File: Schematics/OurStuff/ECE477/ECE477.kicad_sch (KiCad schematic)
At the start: 67 parts, among them J1 USB_B_Micro, J2 Barrel_Jack, J3 OLED JST PH 7pin, J4 Microphone Connector, J5 UART_Conn, J6 Debug Conn, J7 D30V30F3, Q1 SS8050-G, Q2 SS8050-G, SW1 Boot Button, SW2 RST Button, SW3 Button 1, SW4 Button 2, U1 ESP32-WROOM-32E, U2 CP2102N-Axx-xQFN28

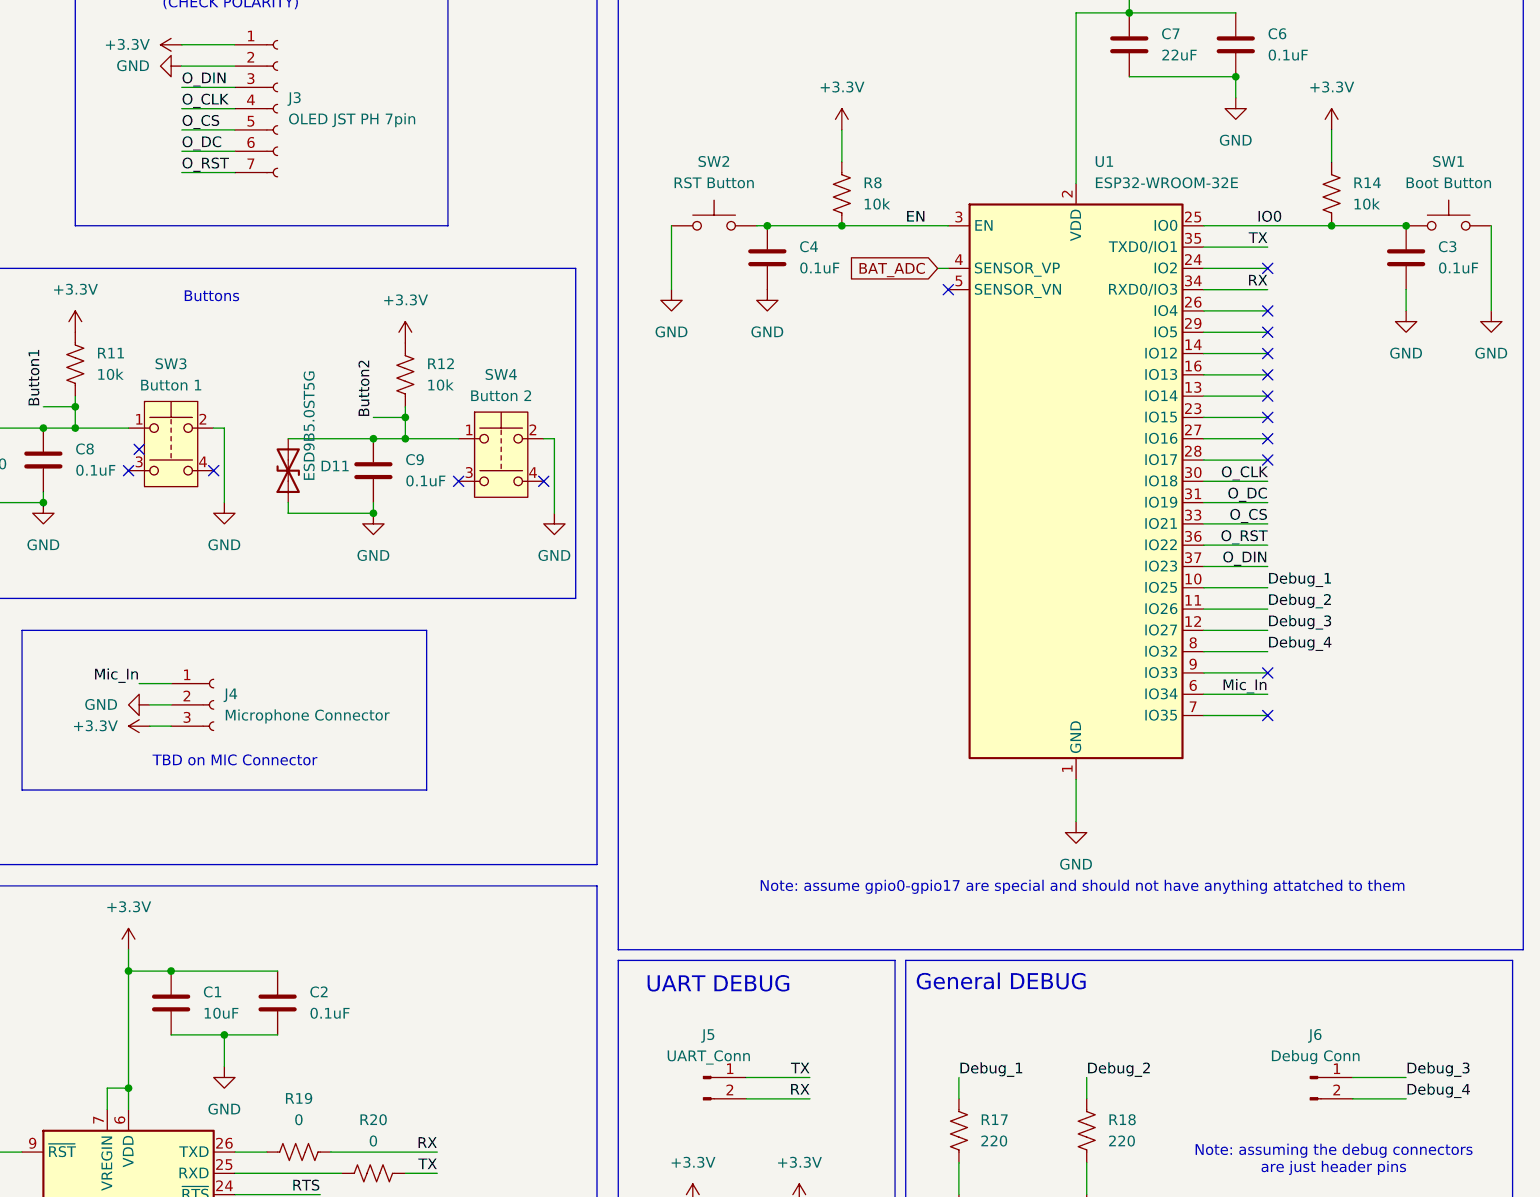
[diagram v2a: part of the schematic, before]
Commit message: Started layout
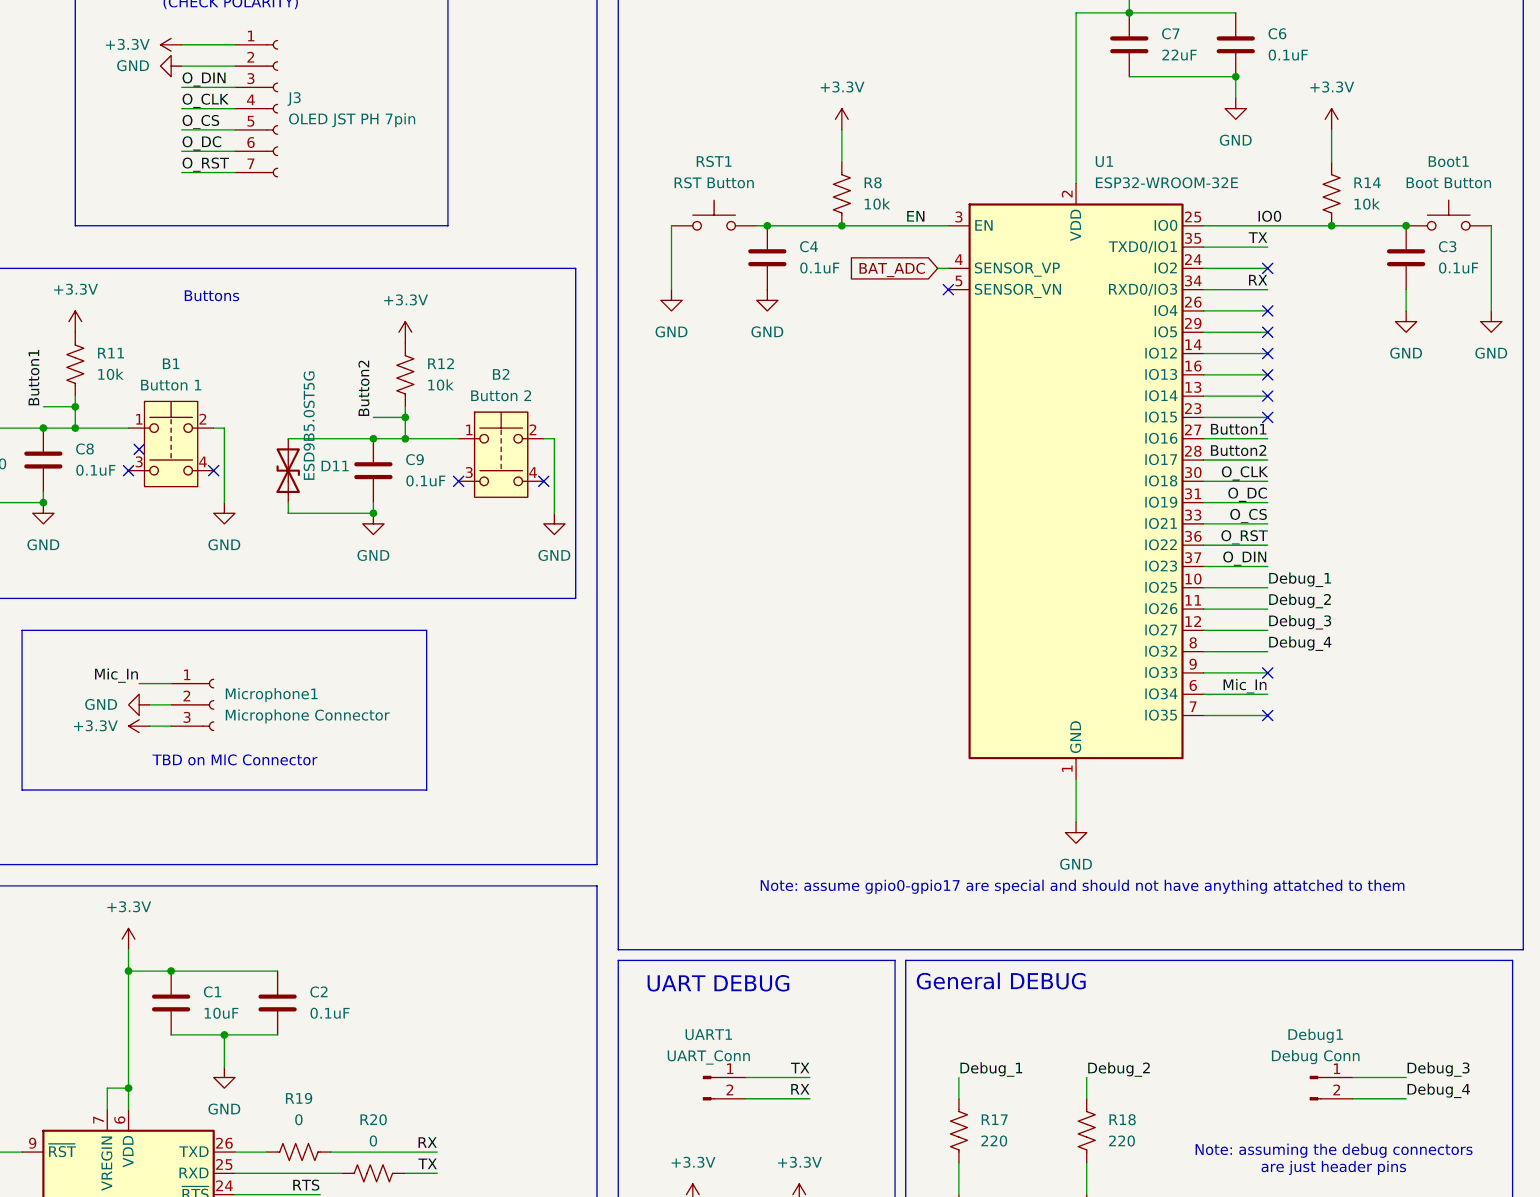
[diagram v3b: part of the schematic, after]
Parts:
- renumbered SW3 to B1, SW4 to B2, SW1 to Boot1, J6 to Debug1, J4 to Microphone1, SW2 to RST1, J5 to UART1
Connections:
- net Button1: now also U1.27 (IO16)
- net Button2: now also U1.28 (IO17)
- no-connect marks 32 -> 30
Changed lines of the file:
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@@
 	)
 	(no_connect
-		(at 375.92 80.01)
-	)
-	(no_connect
 		(at 252.73 208.28)
 	)
@@
 	)
 	(no_connect
-		(at 375.92 82.55)
-	)
-	(no_connect
 		(at 375.92 59.69)
 	)
@@
 		)
 	)
+	(label "Button2"
+		(at 375.92 82.55 180)
+		(fields_autoplaced yes)
+		(effects
+			(font
+				(size 1.27 1.27)
+			)
+			(justify right bottom)
+		)
+	)
 	(label "USB_DN"
 		(at 180.34 219.71 0)
@@
 		)
 	)
+	(label "Button1"
+		(at 375.92 80.01 180)
+		(fields_autoplaced yes)
+		(effects
+			(font
+				(size 1.27 1.27)
+			)
+			(justify right bottom)
+		)
+	)
 	(label "Debug_4"
 		(at 375.92 105.41 0)
@@
 		(dnp no)
 		(fields_autoplaced yes)
-		(property "Reference" "SW1"
+		(property "Reference" "Boot1"
 			(at 397.51 46.99 0)
 			(effects
@@
 			(project ""
 				(path "/f5b3def7-e561-4cb3-8a45-4eba76d025b6"
-					(reference "SW1")
+					(reference "Boot1")
 					(unit 1)
 				)
@@
 		(dnp no)
 		(fields_autoplaced yes)
-		(property "Reference" "SW3"
+		(property "Reference" "B1"
 			(at 245.11 71.12 0)
 			(effects
@@
 			(project ""
 				(path "/f5b3def7-e561-4cb3-8a45-4eba76d025b6"
-					(reference "SW3")
+					(reference "B1")
 					(unit 1)
 				)
@@
 		(dnp no)
 		(fields_autoplaced yes)
-		(property "Reference" "J4"
+		(property "Reference" "Microphone1"
 			(at 251.46 110.4899 0)
 			(effects
@@
 			(project ""
 				(path "/f5b3def7-e561-4cb3-8a45-4eba76d025b6"
-					(reference "J4")
+					(reference "Microphone1")
 					(unit 1)
 				)
@@
 		(dnp no)
 		(fields_autoplaced yes)
-		(property "Reference" "SW4"
+		(property "Reference" "B2"
 			(at 284.48 72.39 0)
 			(effects
@@
 			(project "ECE477"
 				(path "/f5b3def7-e561-4cb3-8a45-4eba76d025b6"
-					(reference "SW4")
+					(reference "B2")
 					(unit 1)
 				)
@@
 		(dnp no)
 		(fields_autoplaced yes)
-		(property "Reference" "J5"
+		(property "Reference" "UART1"
 			(at 309.245 151.13 0)
 			(effects
@@
 			(project ""
 				(path "/f5b3def7-e561-4cb3-8a45-4eba76d025b6"
-					(reference "J5")
+					(reference "UART1")
 					(unit 1)
 				)
@@
 		(dnp no)
 		(fields_autoplaced yes)
-		(property "Reference" "J6"
+		(property "Reference" "Debug1"
 			(at 381.635 151.13 0)
 			(effects
@@
 			(project "ECE477"
 				(path "/f5b3def7-e561-4cb3-8a45-4eba76d025b6"
-					(reference "J6")
+					(reference "Debug1")
 					(unit 1)
 				)
@@
 		(dnp no)
 		(fields_autoplaced yes)
-		(property "Reference" "SW2"
+		(property "Reference" "RST1"
 			(at 309.88 46.99 0)
 			(effects
@@
 			(project "ECE477"
 				(path "/f5b3def7-e561-4cb3-8a45-4eba76d025b6"
-					(reference "SW2")
+					(reference "RST1")
 					(unit 1)
 				)

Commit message: started routing 💢
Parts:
- removed TP10: IO0, TestPoint:TestPoint_Keystone_5010-5014_Multipurpose, symbol Connector:TestPoint
- removed TP9: EN, TestPoint:TestPoint_Keystone_5010-5014_Multipurpose, symbol Connector:TestPoint
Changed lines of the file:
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@@
 	(wire
 		(pts
-			(xy 386.08 243.84) (xy 394.97 243.84)
-		)
-		(stroke
-			(width 0)
-			(type default)
-		)
-	)
-	(wire
-		(pts
 			(xy 368.3 95.25) (xy 375.92 95.25)
 		)
@@
 	(wire
 		(pts
-			(xy 386.08 236.22) (xy 394.97 236.22)
-		)
-		(stroke
-			(width 0)
-			(type default)
-		)
-	)
-	(wire
-		(pts
 			(xy 368.3 100.33) (xy 375.92 100.33)
 		)
@@
 		)
 	)
-	(label "EN"
-		(at 394.97 236.22 180)
-		(fields_autoplaced yes)
-		(effects
-			(font
-				(size 1.27 1.27)
-			)
-			(justify right bottom)
-		)
-	)
 	(label "O_CLK"
 		(at 375.92 85.09 180)
@@
 		)
 	)
-	(label "IO0"
-		(at 394.97 243.84 180)
-		(fields_autoplaced yes)
-		(effects
-			(font
-				(size 1.27 1.27)
-			)
-			(justify right bottom)
-		)
-	)
 	(label "Button1"
 		(at 229.87 76.2 90)
@@
 	)
 	(symbol
-		(lib_id "Connector:TestPoint")
-		(at 386.08 243.84 90)
-		(unit 1)
-		(exclude_from_sim no)
-		(in_bom yes)
-		(on_board yes)
-		(dnp no)
-		(fields_autoplaced yes)
-		(property "Reference" "TP10"
-			(at 382.778 238.76 90)
-			(effects
-				(font
-					(size 1.27 1.27)
-				)
-			)
-		)
-		(property "Value" "IO0"
-			(at 382.778 241.3 90)
-			(effects
-				(font
-					(size 1.27 1.27)
-				)
-			)
-		)
-		(property "Footprint" "TestPoint:TestPoint_Keystone_5010-5014_Multipurpose"
-			(at 386.08 238.76 0)
-			(effects
-				(font
-					(size 1.27 1.27)
-				)
-				(hide yes)
-			)
-		)
-		(property "Datasheet" "~"
-			(at 386.08 238.76 0)
-			(effects
-				(font
-					(size 1.27 1.27)
-				)
-				(hide yes)
-			)
-		)
-		(property "Description" "test point"
-			(at 386.08 243.84 0)
-			(effects
-				(font
-					(size 1.27 1.27)
-				)
-				(hide yes)
-			)
-		)
-		(pin "1"
-		)
-		(instances
-			(project "ECE477"
-				(path "/f5b3def7-e561-4cb3-8a45-4eba76d025b6"
-					(reference "TP10")
-					(unit 1)
-				)
-			)
-		)
-	)
-	(symbol
 		(lib_id "power:GND")
 		(at 265.43 190.5 90)
@@
 					(unit 1)
 				)
-			)
-		)
-	)
-	(symbol
-		(lib_id "Connector:TestPoint")
-		(at 386.08 236.22 90)
-		(unit 1)
-		(exclude_from_sim no)
-		(in_bom yes)
-		(on_board yes)
-		(dnp no)
-		(fields_autoplaced yes)
-		(property "Reference" "TP9"
-			(at 382.778 231.14 90)
-			(effects
-				(font
-					(size 1.27 1.27)
-				)
-			)
-		)
-		(property "Value" "EN"
-			(at 382.778 233.68 90)
-			(effects
-				(font
-					(size 1.27 1.27)
-				)
-			)
-		)
-		(property "Footprint" "TestPoint:TestPoint_Keystone_5010-5014_Multipurpose"
-			(at 386.08 231.14 0)
-			(effects
-				(font
-					(size 1.27 1.27)
-				)
-				(hide yes)
-			)
-		)
-		(property "Datasheet" "~"
-			(at 386.08 231.14 0)
-			(effects
-				(font
-					(size 1.27 1.27)
-				)
-				(hide yes)
-			)
-		)
-		(property "Description" "test point"
-			(at 386.08 236.22 0)
-			(effects
-				(font
-					(size 1.27 1.27)
-				)
-				(hide yes)
-			)
-		)
-		(pin "1"
-		)
-		(instances
-			(project "ECE477"
-				(path "/f5b3def7-e561-4cb3-8a45-4eba76d025b6"
-					(reference "TP9")
-					(unit 1)
-				)

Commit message: hell yeah
pcb complete ver 1 (no more deletes please)
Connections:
- net Gnd_Bat is gone; now on net GND: J2.2, J7.3 (Pin_3)
- net Button1: now also U1.10 (IO25); no longer U1.27 (IO16)
- net Button2: now also U1.11 (IO26); no longer U1.28 (IO17)
- net Debug_1: now also U1.28 (IO17); no longer U1.10 (IO25)
- net Debug_2: now also U1.27 (IO16); no longer U1.11 (IO26)
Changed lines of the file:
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@@
 	)
 	(junction
+		(at 186.69 41.91)
+		(diameter 0)
+		(color 0 0 0 0)
+	)
+	(junction
 		(at 269.24 88.9)
 		(diameter 0)
@@
 	(wire
 		(pts
+			(xy 186.69 41.91) (xy 189.23 41.91)
+		)
+		(stroke
+			(width 0)
+			(type default)
+		)
+	)
+	(wire
+		(pts
 			(xy 240.03 140.97) (xy 240.03 143.51)
 		)
@@
 	(wire
 		(pts
-			(xy 368.3 82.55) (xy 375.92 82.55)
+			(xy 368.3 82.55) (xy 377.19 82.55)
 		)
 		(stroke
@@
 	(wire
 		(pts
-			(xy 368.3 80.01) (xy 375.92 80.01)
+			(xy 368.3 80.01) (xy 377.19 80.01)
 		)
 		(stroke
@@
 	(wire
 		(pts
-			(xy 181.61 41.91) (xy 189.23 41.91)
+			(xy 181.61 41.91) (xy 186.69 41.91)
 		)
 		(stroke
@@
 	(label "RX"
 		(at 375.92 62.23 180)
-		(fields_autoplaced yes)
-		(effects
-			(font
-				(size 1.27 1.27)
-			)
-			(justify right bottom)
-		)
-	)
-	(label "Button2"
-		(at 375.92 82.55 180)
-		(fields_autoplaced yes)
 		(effects
 			(font
@@
 	(label "USB_DN"
 		(at 180.34 219.71 0)
-		(fields_autoplaced yes)
 		(effects
 			(font
@@
 	(label "TX"
 		(at 321.31 156.21 180)
-		(fields_autoplaced yes)
 		(effects
 			(font
@@
 	(label "TXT"
 		(at 307.34 195.58 180)
-		(fields_autoplaced yes)
 		(effects
 			(font
@@
 	(label "O_DC"
 		(at 375.92 87.63 180)
-		(fields_autoplaced yes)
 		(effects
 			(font
@@
 	(label "RXT"
 		(at 320.04 195.58 180)
-		(fields_autoplaced yes)
 		(effects
 			(font
@@
 	(label "Debug_2"
 		(at 354.33 156.21 0)
-		(fields_autoplaced yes)
 		(effects
 			(font
@@
 	(label "O_DIN"
 		(at 246.38 38.1 0)
-		(fields_autoplaced yes)
 		(effects
 			(font
@@
 	(label "RX"
 		(at 321.31 158.75 180)
-		(fields_autoplaced yes)
 		(effects
 			(font
@@
 		)
 	)
-	(label "Button1"
-		(at 375.92 80.01 180)
-		(fields_autoplaced yes)
+	(label "Debug_4"
+		(at 375.92 105.41 0)
 		(effects
 			(font
 				(size 1.27 1.27)
 			)
-			(justify right bottom)
+			(justify left bottom)
 		)
 	)
-	(label "Debug_4"
-		(at 375.92 105.41 0)
-		(fields_autoplaced yes)
+	(label "Debug_1"
+		(at 377.19 82.55 180)
 		(effects
 			(font
 				(size 1.27 1.27)
 			)
-			(justify left bottom)
+			(justify right bottom)
 		)
 	)
 	(label "Debug_4"
 		(at 392.43 158.75 0)
-		(fields_autoplaced yes)
 		(effects
 			(font
@@
 	(label "USB_DP"
 		(at 191.77 217.17 0)
-		(fields_autoplaced yes)
 		(effects
 			(font
@@
 	(label "Mic_In"
 		(at 375.92 110.49 180)
-		(fields_autoplaced yes)
 		(effects
 			(font
@@
 	(label "EN"
 		(at 342.9 208.28 180)
-		(fields_autoplaced yes)
+		(effects
+			(font
+				(size 1.27 1.27)
+			)
+			(justify right bottom)
+		)
+	)
+	(label "Button1"
+		(at 375.92 97.79 180)
 		(effects
 			(font
@@
 	(label "O_CLK"
 		(at 375.92 85.09 180)
-		(fields_autoplaced yes)
 		(effects
 			(font
@@
 	(label "Debug_3"
 		(at 392.43 156.21 0)
-		(fields_autoplaced yes)
 		(effects
 			(font
@@
 	(label "TX"
 		(at 276.86 167.64 180)
-		(fields_autoplaced yes)
 		(effects
 			(font
@@
 	(label "RTS"
 		(at 262.89 170.18 180)
-		(fields_autoplaced yes)
 		(effects
 			(font
@@
 	(label "Debug_1"
 		(at 339.09 156.21 0)
-		(fields_autoplaced yes)
 		(effects
 			(font
@@
 	(label "RX"
 		(at 276.86 165.1 180)
-		(fields_autoplaced yes)
 		(effects
 			(font
@@
 	(label "IO0"
 		(at 374.65 54.61 0)
-		(fields_autoplaced yes)
 		(effects
 			(font
@@
 	(label "O_DC"
 		(at 246.38 45.72 0)
-		(fields_autoplaced yes)
 		(effects
 			(font
@@
 	(label "O_RST"
 		(at 375.92 92.71 180)
-		(fields_autoplaced yes)
 		(effects
 			(font
@@
 		)
 	)
-	(label "Debug_1"
-		(at 375.92 97.79 0)
-		(fields_autoplaced yes)
-		(effects
-			(font
-				(size 1.27 1.27)
-			)
-			(justify left bottom)
-		)
-	)
 	(label "Debug_3"
 		(at 375.92 102.87 0)
-		(fields_autoplaced yes)
 		(effects
 			(font
@@
 	(label "DTR"
 		(at 299.72 215.9 0)
-		(fields_autoplaced yes)
 		(effects
 			(font
@@
 	(label "O_CS"
 		(at 375.92 90.17 180)
-		(fields_autoplaced yes)
 		(effects
 			(font
@@
 	(label "O_CLK"
 		(at 246.38 40.64 0)
-		(fields_autoplaced yes)
 		(effects
 			(font
@@
 		)
 	)
+	(label "Debug_2"
+		(at 377.19 80.01 180)
+		(effects
+			(font
+				(size 1.27 1.27)
+			)
+			(justify right bottom)
+		)
+	)
 	(label "Button2"
 		(at 269.24 77.47 90)
-		(fields_autoplaced yes)
 		(effects
 			(font
@@
 	(label "O_RST"
 		(at 246.38 48.26 0)
-		(fields_autoplaced yes)
 		(effects
 			(font
@@
 		)
 	)
+	(label "Button2"
+		(at 375.92 100.33 180)
+		(effects
+			(font
+				(size 1.27 1.27)
+			)
+			(justify right bottom)
+		)
+	)
 	(label "Mic_In"
 		(at 393.7 220.98 180)
-		(fields_autoplaced yes)
 		(effects
 			(font
@@
 	(label "DTR"
 		(at 262.89 177.8 180)
-		(fields_autoplaced yes)
 		(effects
 			(font
@@
 	(label "EN"
 		(at 332.74 54.61 0)
-		(fields_autoplaced yes)
 		(effects
 			(font
@@
 	(label "USB_DN"
 		(at 214.63 180.34 0)
-		(fields_autoplaced yes)
 		(effects
 			(font
@@
 	(label "RXT"
 		(at 266.7 198.12 180)
-		(fields_autoplaced yes)
 		(effects
 			(font
@@
 	(label "Mic_In"
 		(at 241.3 109.22 180)
-		(fields_autoplaced yes)
 		(effects
 			(font
@@
 	(label "TXT"
 		(at 266.7 195.58 180)
-		(fields_autoplaced yes)
 		(effects
 			(font
@@
 	(label "Button1"
 		(at 229.87 76.2 90)
-		(fields_autoplaced yes)
 		(effects
 			(font
@@
 	(label "TX"
 		(at 375.92 57.15 180)
-		(fields_autoplaced yes)
 		(effects
 			(font
@@
 		)
 	)
-	(label "Debug_2"
-		(at 375.92 100.33 0)
-		(fields_autoplaced yes)
-		(effects
-			(font
-				(size 1.27 1.27)
-			)
-			(justify left bottom)
-		)
-	)
 	(label "O_DIN"
 		(at 375.92 95.25 180)
-		(fields_autoplaced yes)
 		(effects
 			(font
@@
 	(label "RTS"
 		(at 299.72 238.76 0)
-		(fields_autoplaced yes)
 		(effects
 			(font
@@
 	(label "IO0"
 		(at 344.17 233.68 180)
-		(fields_autoplaced yes)
 		(effects
 			(font
@@
 	(label "USB_DP"
 		(at 214.63 182.88 0)
-		(fields_autoplaced yes)
 		(effects
 			(font
@@
 	(label "O_CS"
 		(at 246.38 43.18 0)
-		(fields_autoplaced yes)
 		(effects
 			(font
@@
 					(unit 1)
 				)
+			)
+		)
+	)
+	(symbol
+		(lib_id "power:GND")
+		(at 186.69 41.91 0)
+		(unit 1)
+		(exclude_from_sim no)
+		(in_bom yes)
+		(on_board yes)
+		(dnp no)
+		(fields_autoplaced yes)
+		(property "Reference" "#PWR044"
+			(at 186.69 48.26 0)
+			(effects
+				(font
+					(size 1.27 1.27)
+				)
+				(hide yes)
+			)
+		)
+		(property "Value" "GND"
+			(at 186.69 46.99 0)
+			(effects
+				(font
+					(size 1.27 1.27)
+				)
+			)
+		)
+		(property "Footprint" ""
+			(at 186.69 41.91 0)
+			(effects
+				(font
+					(size 1.27 1.27)
+				)
+				(hide yes)
+			)
+		)
+		(property "Datasheet" ""
+			(at 186.69 41.91 0)
+			(effects
+				(font
+					(size 1.27 1.27)
+				)
+				(hide yes)
+			)
+		)
+		(property "Description" "Power symbol creates a global label with name \"GND\" , ground"
+			(at 186.69 41.91 0)
+			(effects
+				(font
+					(size 1.27 1.27)
+				)
+				(hide yes)
+			)
+		)
+		(pin "1"
+		)
+		(instances
+			(project "ECE477"
+				(path "/f5b3def7-e561-4cb3-8a45-4eba76d025b6"
+					(reference "#PWR044")
+					(unit 1)
+				)
